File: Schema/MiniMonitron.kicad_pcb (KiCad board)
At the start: 2 copper layers, 165 x 1.5 mm, 41 parts, among them J1 CONN_01X02, J10 CONN_01X02, J2 CONN_02X20, J3 CONN_02X20, J4 CONN_01X02, J5 CONN_01X02, J6 CONN_01X02, J7 CONN_01X02, J8 CONN_01X02, J9 CONN_01X02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

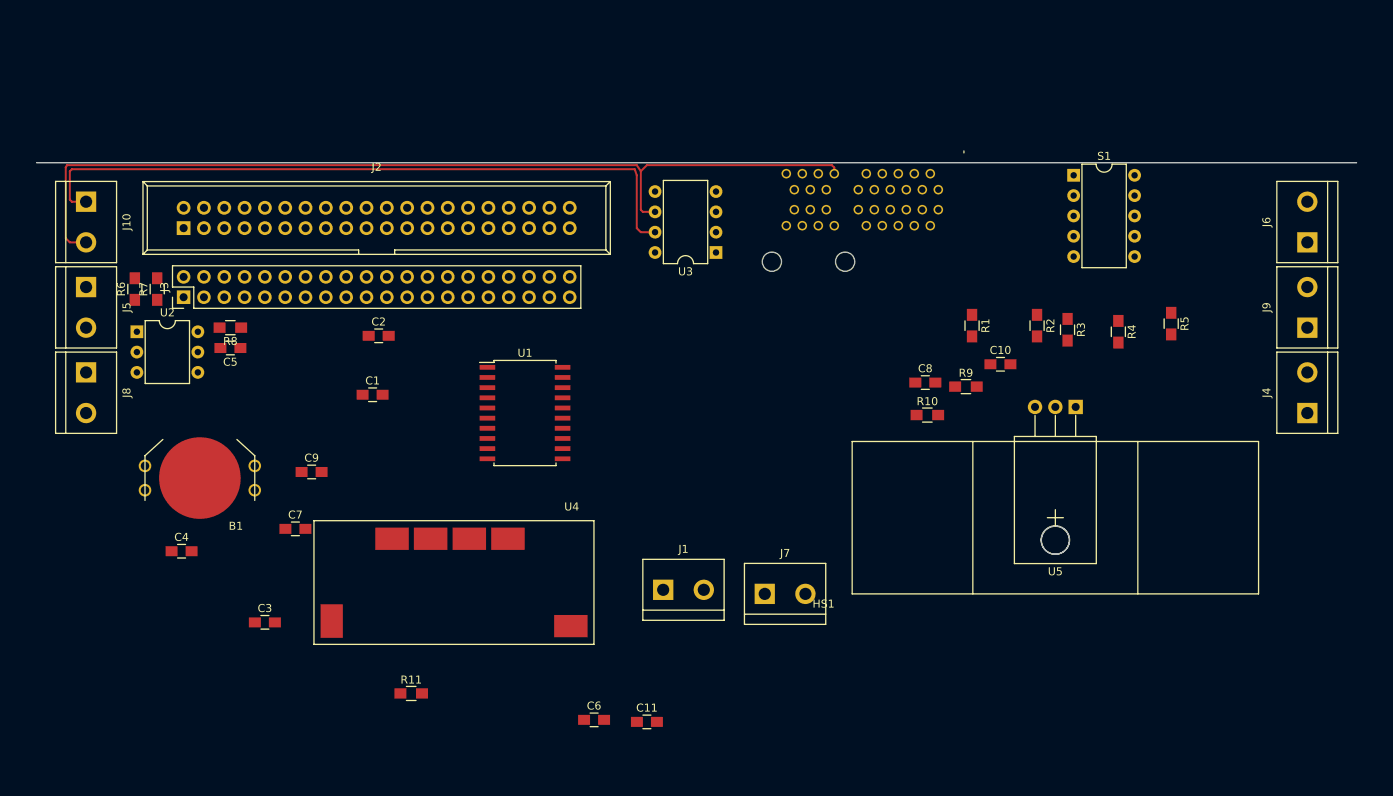
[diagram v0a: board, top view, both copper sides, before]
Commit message: Placement des pièces sur le PCB + commencement du routage
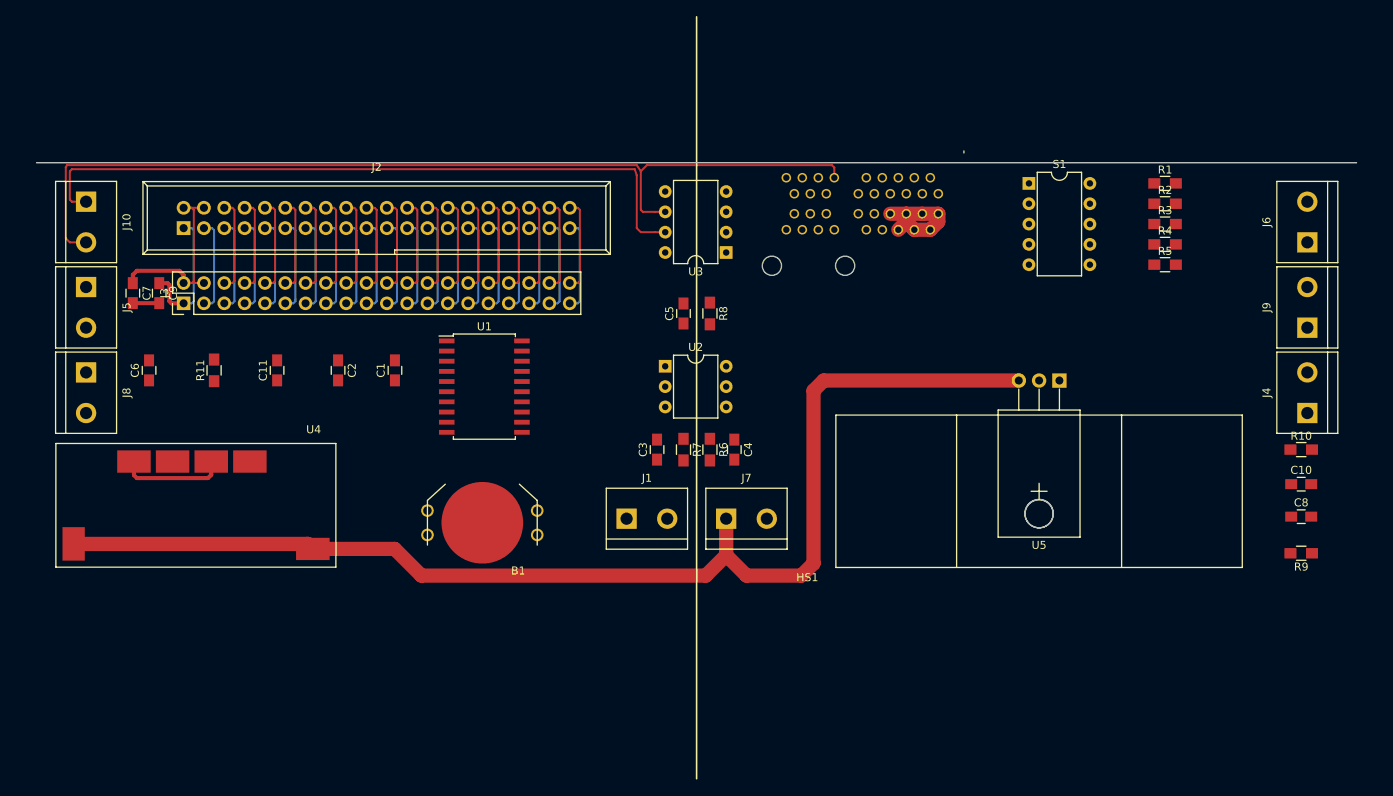
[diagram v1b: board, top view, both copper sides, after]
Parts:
- moved R6 74.6 mm to (152.4, 71.4), turned to 270 degrees
- moved C6 70.7 mm to (82.3, 61.5), turned to 90 degrees
- moved C4 70.2 mm to (155.4, 71.4), turned to 270 degrees
- moved R7 68.8 mm to (149.1, 71.4), turned to 270 degrees
- moved U2 66.2 mm to (146.8, 61.0)
- moved C11 63.8 mm to (98.3, 61.5), turned to 90 degrees
- moved R8 60.0 mm to (152.4, 54.4), turned to 270 degrees
- moved C5 56.8 mm to (149.1, 54.4), turned to 90 degrees
- moved C3 53.6 mm to (145.8, 71.4), turned to 90 degrees
- moved C8 49.9 mm to (226.3, 79.8)
- moved R11 47.3 mm to (90.4, 61.5), turned to 90 degrees
- moved R10 46.9 mm to (226.3, 71.4)
- moved R9 46.8 mm to (226.3, 84.3), turned to 180 degrees
- moved C10 40.5 mm to (226.3, 75.7)
- moved C7 35.8 mm to (80.3, 51.8), turned to 270 degrees
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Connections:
- C3 pad 2: 3V3_pwr -> +3V3
- J2 pad 1: 3V3_pwr -> +3V3
- J3 pad 1: 3V3_pwr -> +3V3
- U1 pad 20: 3V3_pwr -> +3V3
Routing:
- net +24V: track 0.00 -> 163.5 mm
- net GND: track 0.00 -> 96.4 mm
- net +5V: track 0.00 -> 38.9 mm
- net +3V3: track 0.00 -> 16.9 mm
- net UART_TX: track 0.00 -> 11.6 mm
- net SPI_MISO: track 0.00 -> 11.6 mm
- net SPI_CE1: track 0.00 -> 11.6 mm
- net PCM_CLK: track 0.00 -> 11.6 mm
- net I2C_SDA: track 0.00 -> 11.6 mm
- net GPIO4: track 0.00 -> 11.6 mm
- net GPIO25: track 0.00 -> 11.6 mm
- net CPIO17: track 0.00 -> 11.6 mm
- net GPIO26: track 0.00 -> 11.6 mm
- net GPIO21: track 0.00 -> 11.6 mm
- net GPIO20: track 0.00 -> 11.6 mm
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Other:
- net class Default: trace_width 0.25 -> 0.3048

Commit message: PCB terminé et envoyé, fichiers gerber crées + création du dossier Documentations avec le document du manuel technique
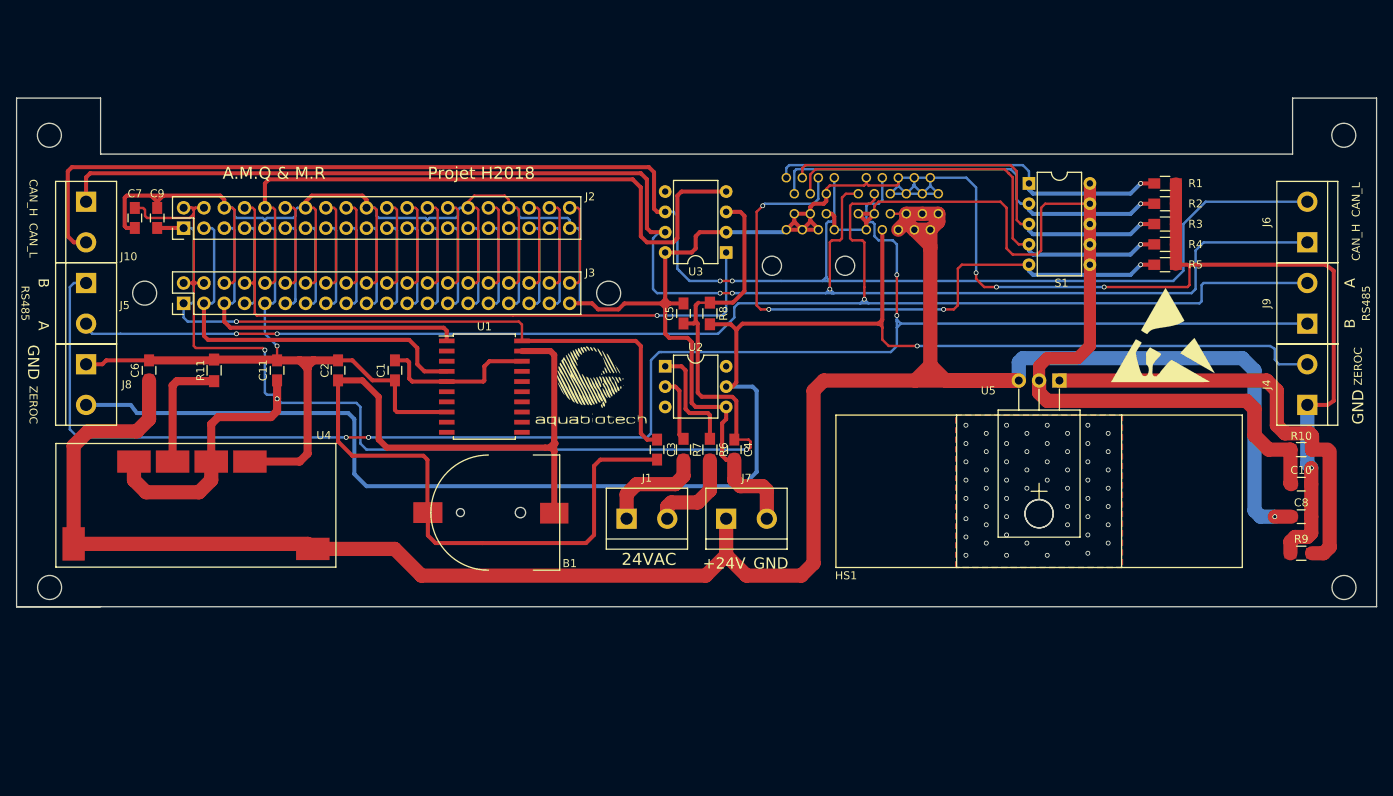
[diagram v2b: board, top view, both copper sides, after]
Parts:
- added G***: LOGO, mini_monitron:AquaLogo, F.Cu at (137.5, 63.5)
- added REF**: Percage, mini_monitron:Percage, F.Cu at (72.1, 31.2)
- added REF**: Percage, mini_monitron:Percage, F.Cu at (232.9, 30.5)
- added REF**: Percage, mini_monitron:Percage, F.Cu at (81.5, 51.1)
- added REF**: Percage, mini_monitron:Percage, F.Cu at (142.0, 51.1)
- added REF**: Percage, mini_monitron:Percage, F.Cu at (231.6, 88.6)
- added REF**: Percage, mini_monitron:Percage, F.Cu at (69.8, 88.6)
- added REF***: ESD-Logo_13.2x12mm_SilkScreen, Symbols:ESD-Logo_13.2x12mm_SilkScreen, F.Cu at (209.0, 57.0)
- B1: footprint mini_monitron:keystone_1220 -> mini_monitron:Keystone_CR1220_SMD
- J2: footprint mini_monitron:IDC_Header_Straight_40pins -> mini_monitron:Pin_Header_Straight_2x20_Pitch2.54mm
- moved C7 9.40 mm to (80.5, 42.4)
- moved C9 9.40 mm to (83.3, 42.4), turned to 90 degrees
- moved B1 1.48 mm to (124.7, 79.2)
- moved J4 1.02 mm to (227.1, 63.2)
- moved J8 1.02 mm to (74.4, 63.2)
- moved J5 0.51 mm to (74.4, 53.1)
- moved J9 0.51 mm to (227.1, 53.1)
- turned J2 to 90 degrees
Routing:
- net GND: track 96.4 -> 557.7 mm, vias 0 -> 5
- net RS485_B: track 0.00 -> 211.9 mm, vias 0 -> 4
- net ZERO_CROSS: track 0.00 -> 206.8 mm, vias 0 -> 1
- net RS485_A: track 0.00 -> 176.7 mm, vias 0 -> 3
- net +5V: track 38.9 -> 192.7 mm, vias 0 -> 3
- net 5V_pwr_MODULE: track 0.00 -> 124.0 mm
- net +24V: track 163.5 -> 281.0 mm, vias 0 -> 1
- net CAN_H: track 87.6 -> 194.5 mm, vias 0 -> 3
- net CAN_L: track 117.9 -> 201.3 mm, vias 0 -> 2
- net Net-(P1-PadA14): track 0.00 -> 79.1 mm, vias 0 -> 4
- net UART_RX: track 11.6 -> 85.1 mm
- net +3V3: track 16.9 -> 89.8 mm, vias 0 -> 1
- net UART_TX: track 11.6 -> 82.7 mm, vias 0 -> 1
- net Net-(B1-Pad2): track 0.00 -> 67.1 mm
- net Net-(P1-PadA15): track 0.00 -> 55.5 mm, vias 0 -> 1
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- added copper zone on B.Cu, net (none)
- added copper zone on F.Cu, net (none)
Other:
- board size 165 x 1.5 mm -> 170 x 63.6 mm
- board text added: "+24V"
- board text added: "24VAC"
- board text added: "A"
- board text added: "A.M.Q & M.R"
- board text added: "B"
- board text added: "CAN_H"
- board text added: "CAN_L"
- board text added: "GND"
- board text added: "Projet H2018"
- board text added: "RS485"
- board text added: "ZEROC"

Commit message: Correction du PCB + nouveau fichier Gerber
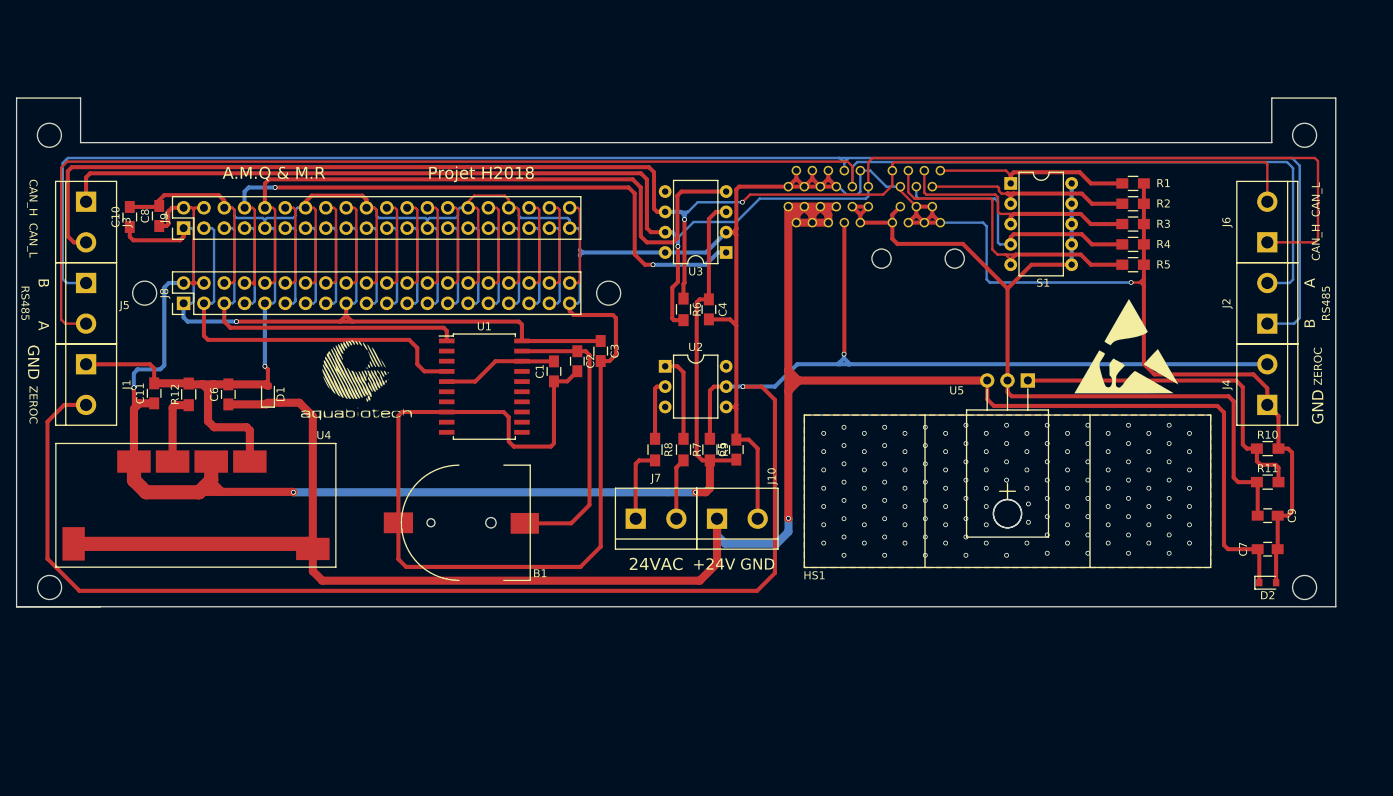
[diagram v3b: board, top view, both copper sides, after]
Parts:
- added D1: D, mini_monitron:D_0805, F.Cu at (97.2, 64.5)
- added D2: D, mini_monitron:D_0805, F.Cu at (222.1, 88.0)
- added R12: 4.3k, mini_monitron:R_0805_HandSoldering, F.Cu at (87.2, 64.5)
- C10, C8: value 10uF -> 0.1uf
- C7, C9: value 0.1uf -> 10uF
- J2, J3: value CONN_02X20 -> CONN_01X02; footprint mini_monitron:Pin_Header_Straight_2x20_Pitch2.54mm -> mini_monitron:bornier2
- J8, J9: value CONN_01X02 -> CONN_02X20; footprint mini_monitron:bornier2 -> mini_monitron:Pin_Header_Straight_2x20_Pitch2.54mm
- P1: footprint mini_monitron:pci-x_conn-x1_Vertical -> mini_monitron:pci-x_conn-x1_Vertical_back; moved to F.Cu
- R10: value 100 -> 300
- R11: value 4.3k -> 100
- R6: value 1k -> 120
- R9: value 300 -> 1k
- moved C10 150.2 mm to (79.9, 42.3), turned to 90 degrees
- moved C8 147.6 mm to (83.6, 42.2), turned to 90 degrees
- moved C7 147.5 mm to (222.1, 83.8), turned to 0 degrees
- moved C9 143.7 mm to (222.1, 79.6), turned to 0 degrees
- moved J9 140.8 mm to (86.6, 43.7)
- moved J2 135.8 mm to (222.1, 53.1)
- moved R11 132.4 mm to (222.1, 75.4), turned to 0 degrees
- moved J10 89.5 mm to (155.8, 80.0), turned to 0 degrees
- moved R9 75.0 mm to (152.4, 71.4), turned to 90 degrees
- moved J1 72.1 mm to (74.4, 63.2), turned to 270 degrees
- moved C2 29.9 mm to (135.8, 60.3), turned to 90 degrees
- moved G*** 29.3 mm to (108.2, 62.7)
- moved C1 19.9 mm to (132.9, 61.6)
- moved R8 18.3 mm to (145.5, 71.4)
- moved C5 18.3 mm to (155.7, 71.4)
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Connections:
- C10 pad 1: 5V_pwr_MODULE -> +3V3
- C7 pad 1: +5V -> +24V
- C8 pad 1: +24V -> +5V
- C9 pad 1: +3V3 -> 5V_pwr_MODULE
- J1 pad 1: /24VAC_2F -> GND
- J1 pad 2: /24VAC_1F -> ZERO_CROSS
- J10 pad 1: CAN_H -> +24V
- J10 pad 2: CAN_L -> GND
- J2 pad 1: +3V3 -> RS485_B
- J2 pad 2: +5V -> RS485_A
- J3 pad 1: +3V3 -> CAN_H
- J3 pad 2: +5V -> CAN_L
- J7 pad 1: +24V -> /24VAC_2F
- J7 pad 2: GND -> /24VAC_1F
- J8 pad 1: GND -> +3V3
- J8 pad 2: ZERO_CROSS -> +5V
- J9 pad 1: RS485_B -> +3V3
- J9 pad 2: RS485_A -> +5V
- R10 pad 1: 5V_pwr_MODULE -> Net-(R10-Pad1)
- R10 pad 2: Net-(R10-Pad2) -> GND
- R11 pad 1: Net-(R11-Pad1) -> 5V_pwr_MODULE
- R11 pad 2: GND -> Net-(R10-Pad1)
- R6 pad 1: Net-(R6-Pad1) -> CAN_L
- R6 pad 2: /24VAC_1F -> CAN_H
- R7 pad 2: /24VAC_2F -> /24VAC_1F
- R8 pad 1: +5V -> Net-(R8-Pad1)
- R8 pad 2: ZERO_CROSS -> /24VAC_2F
- R9 pad 1: Net-(R10-Pad2) -> +5V
- R9 pad 2: GND -> ZERO_CROSS
- U1 pad 10: Net-(U1-Pad10) -> (no net)
- U1 pad 11: Net-(U1-Pad11) -> (no net)
- U1 pad 12: Net-(U1-Pad12) -> (no net)
- U1 pad 13: Net-(U1-Pad13) -> (no net)
- U1 pad 14: Net-(U1-Pad14) -> (no net)
- U1 pad 15: Net-(U1-Pad15) -> (no net)
- U1 pad 16: Net-(U1-Pad16) -> (no net)
- U1 pad 17: Net-(U1-Pad17) -> (no net)
- U1 pad 2: Net-(U1-Pad2) -> (no net)
- U1 pad 3: Net-(U1-Pad3) -> (no net)
- U1 pad 6: Net-(U1-Pad6) -> (no net)
- U1 pad 7: Net-(U1-Pad7) -> (no net)
- U1 pad 9: Net-(U1-Pad9) -> (no net)
- U2 pad 1: Net-(R6-Pad1) -> Net-(R7-Pad1)
- U2 pad 2: Net-(R7-Pad1) -> Net-(R8-Pad1)
- U2 pad 3: Net-(U2-Pad3) -> (no net)
- U2 pad 6: Net-(U2-Pad6) -> (no net)
- U3 pad 5: Net-(U3-Pad5) -> (no net)
- U4 pad 5: Net-(R11-Pad1) -> Net-(R12-Pad1)
- U5 pad 1: Net-(R10-Pad2) -> Net-(R10-Pad1)
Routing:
- net Net-(R10-Pad2): track 55.4 -> 0.00 mm
- net Net-(R10-Pad1): track 0.00 -> 42.8 mm
- net Net-(P1-PadA14): track 79.1 -> 39.9 mm, vias 4 -> 0
- net ZERO_CROSS: track 206.8 -> 239.7 mm, vias 1 -> 2
- net Net-(B1-Pad2): track 67.1 -> 35.4 mm
- net Net-(P1-PadA17): track 53.0 -> 26.9 mm, vias 1 -> 0
- net Net-(P1-PadA18): track 50.7 -> 24.7 mm, vias 1 -> 0
- net RS485_A: track 176.7 -> 199.7 mm, vias 3 -> 0
- net Net-(P1-PadA16): track 53.5 -> 31.6 mm, vias 1 -> 0
- net Net-(P1-PadA15): track 55.5 -> 34.0 mm, vias 1 -> 0
- net +5V: track 192.7 -> 176.7 mm
- net Net-(R11-Pad1): track 14.9 -> 0.00 mm
- net 5V_pwr_MODULE: track 124.0 -> 109.2 mm
- net CAN_L: track 201.3 -> 186.6 mm
- net Net-(R6-Pad1): track 13.9 -> 0.00 mm
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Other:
- board size 170 x 63.6 mm -> 164.9 x 63.6 mm
- net class Default: trace_width 0.3048 -> 0.508

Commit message: PCB final + avancement du manuel technique
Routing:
- net (no net): track 0.00 -> 62.9 mm
- net RS485_A: track 199.7 -> 226.2 mm, vias 0 -> 1
- net ZERO_CROSS: track 239.7 -> 258.7 mm, vias 2 -> 1
- net CAN_L: track 186.6 -> 195.5 mm, vias 2 -> 1
- net 5V_pwr_MODULE: track 109.2 -> 116.6 mm
- net CAN_H: track 199.8 -> 194.3 mm
- net +24V: track 276.4 -> 281.0 mm
- net Net-(P1-PadA14): track 39.9 -> 35.3 mm
- net Net-(P1-PadA17): track 26.9 -> 31.2 mm
- net Net-(P1-PadA18): track 24.7 -> 29.1 mm
- net RS485_B: track 199.0 -> 203.1 mm, vias 0 -> 1
- net Net-(P1-PadA16): track 31.6 -> 29.3 mm
- net Net-(P1-PadA15): track 34.0 -> 31.8 mm
- net GND: track 555.0 -> 554.5 mm, vias 2 -> 1
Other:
- net class heatsink added: clearance 0, trace_width 0.508, via_dia 0.6, via_drill 0.4
- board text added: "+"
- board text added: "-"
- board text added: "°"

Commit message: Avancement des corrections du manuel technique + ajout photos et screenshots
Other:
- board text added: "40pins test"
- board text added: "Raspberry PI"
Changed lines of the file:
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@@
     (links 170)
     (no_connects 0)
-    (area 65.660999 27.356999 230.711001 91.091001)
+    (area 60.554 19.345 245.928858 91.14408)
     (thickness 1.6)
-    (drawings 34)
+    (drawings 36)
     (tracks 985)
     (zones 0)
@@
     )
   )
+  (gr_text "Raspberry PI" (at 108.204 47.244) (layer F.SilkS)
+    (effects (font (size 1.5 1.5) (thickness 0.3)))
+  )
+  (gr_text "40pins test" (at 108.204 37.338) (layer F.SilkS)
+    (effects (font (size 1.5 1.5) (thickness 0.3)))
+  )
   (gr_text ° (at 84.4296 46.42104) (layer F.SilkS)
     (effects (font (size 1.5 1.5) (thickness 0.3)))
@@
     (effects (font (size 1.5 1.5) (thickness 0.3)))
   )
-  (gr_text "Projet H2018" (at 123.825 36.83) (layer F.SilkS)
+  (gr_text "Projet H2018" (at 169.164 62.992) (layer F.SilkS)
     (effects (font (size 1.5 1.5) (thickness 0.3)))
   )
-  (gr_text "A.M.Q & M.R" (at 97.917 36.83) (layer F.SilkS)
+  (gr_text "A.M.Q & M.R" (at 168.91 58.674) (layer F.SilkS)
     (effects (font (size 1.5 1.5) (thickness 0.3)))
   )
